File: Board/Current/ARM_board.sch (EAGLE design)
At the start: 177 parts, among them IC3 STM32F437VI, IC4 LM358DT, J1 USART/I2C, J10 ANALOG, J11 DGND, J12 DPWR, J13 DIGITAL, J14 SGND, J15 SPWR, J16 SERVO, J2 I2C2/USART3, J3 USART2, J5 SPI, J6 Bluesmirf, J7 SWD, J8 AGND, J9 APWR, Q1 STL4P2UH7, Q2 2STR1230, Q3 STL4P2UH7, SW1 SW, U1 LSM330, U10 BAV99, U11 BAV99, U12 USBLC6-2, U13 USBLC6-2, U14 STMPS2171MTR, U15 MC74HC164, U3 NC7SZU04, U4 L6206Q, U5 L6206Q, U6 SI7617, U7 SI7617, U8 SI7617, U9 SI7617, Y2 8MHz

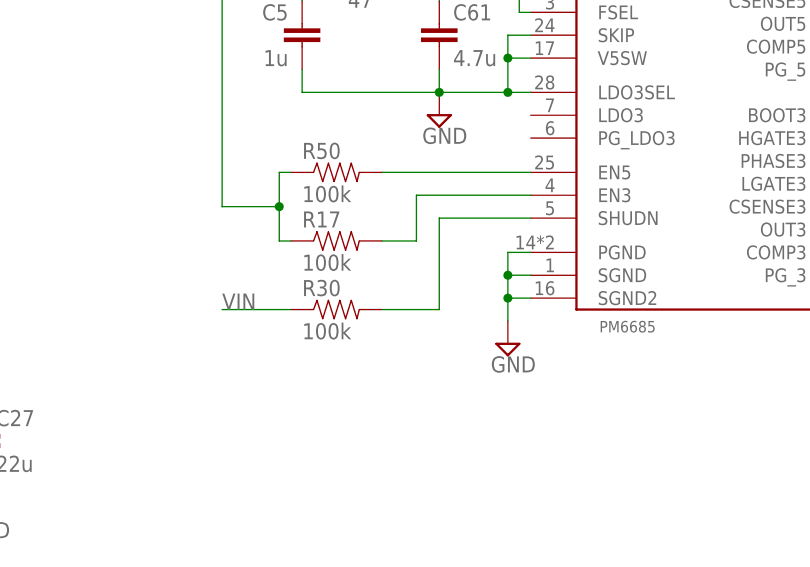
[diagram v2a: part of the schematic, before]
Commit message: Fixed the size of the 680uF capacitors. Added new voltage divider on SHDWN pin of switching controller.
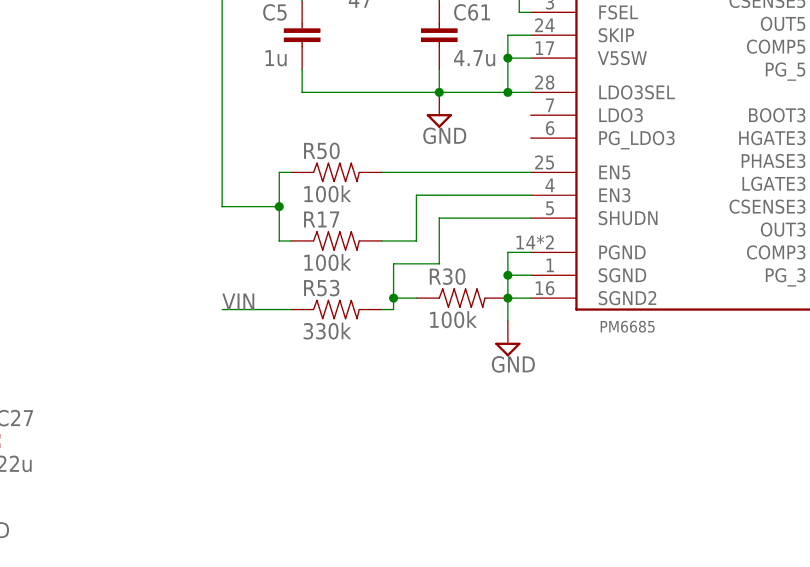
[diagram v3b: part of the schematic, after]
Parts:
- added R53: 330k, SparkFun:RESISTOR0402-RES
- C44, C52: device SparkFun:CAP_POLD -> SparkFun:CAP_POLE
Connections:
- net GND: now also R30.2
- net N$82: now also R30.1, R53.2; no longer R30.2
- net VIN: now also R53.1; no longer R30.1
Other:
- moved on the sheet: R30
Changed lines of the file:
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@@
 <grid distance="0.05" unitdist="inch" unit="inch" style="lines" multiple="1" display="no" altdistance="0.01" altunitdist="inch" altunit="inch"/>
 <layers>
-<layer number="1" name="Top" color="4" fill="1" visible="no" active="no"/>
-<layer number="16" name="Bottom" color="1" fill="1" visible="no" active="no"/>
-<layer number="17" name="Pads" color="2" fill="1" visible="no" active="no"/>
-<layer number="18" name="Vias" color="2" fill="1" visible="no" active="no"/>
-<layer number="19" name="Unrouted" color="6" fill="1" visible="no" active="no"/>
-<layer number="20" name="Dimension" color="15" fill="1" visible="no" active="no"/>
-<layer number="21" name="tPlace" color="15" fill="1" visible="no" active="no"/>
-<layer number="22" name="bPlace" color="7" fill="1" visible="no" active="no"/>
-<layer number="23" name="tOrigins" color="15" fill="1" visible="no" active="no"/>
-<layer number="24" name="bOrigins" color="15" fill="1" visible="no" active="no"/>
-<layer number="25" name="tNames" color="15" fill="1" visible="no" active="no"/>
-<layer number="26" name="bNames" color="7" fill="1" visible="no" active="no"/>
-<layer number="27" name="tValues" color="7" fill="1" visible="no" active="no"/>
-<layer number="28" name="bValues" color="7" fill="1" visible="no" active="no"/>
+<layer number="1" name="Top" color="4" fill="1" visible="yes" active="no"/>
+<layer number="16" name="Bottom" color="1" fill="1" visible="yes" active="no"/>
+<layer number="17" name="Pads" color="2" fill="1" visible="yes" active="no"/>
+<layer number="18" name="Vias" color="2" fill="1" visible="yes" active="no"/>
+<layer number="19" name="Unrouted" color="6" fill="1" visible="yes" active="no"/>
+<layer number="20" name="Dimension" color="15" fill="1" visible="yes" active="no"/>
+<layer number="21" name="tPlace" color="15" fill="1" visible="yes" active="no"/>
+<layer number="22" name="bPlace" color="7" fill="1" visible="yes" active="no"/>
+<layer number="23" name="tOrigins" color="15" fill="1" visible="yes" active="no"/>
+<layer number="24" name="bOrigins" color="15" fill="1" visible="yes" active="no"/>
+<layer number="25" name="tNames" color="15" fill="1" visible="yes" active="no"/>
+<layer number="26" name="bNames" color="7" fill="1" visible="yes" active="no"/>
+<layer number="27" name="tValues" color="7" fill="1" visible="yes" active="no"/>
+<layer number="28" name="bValues" color="7" fill="1" visible="yes" active="no"/>
 <layer number="29" name="tStop" color="7" fill="3" visible="no" active="no"/>
 <layer number="30" name="bStop" color="7" fill="6" visible="no" active="no"/>
@@
 <layer number="35" name="tGlue" color="7" fill="4" visible="no" active="no"/>
 <layer number="36" name="bGlue" color="7" fill="5" visible="no" active="no"/>
-<layer number="37" name="tTest" color="7" fill="1" visible="no" active="no"/>
-<layer number="38" name="bTest" color="7" fill="1" visible="no" active="no"/>
+<layer number="37" name="tTest" color="7" fill="1" visible="yes" active="no"/>
+<layer number="38" name="bTest" color="7" fill="1" visible="yes" active="no"/>
 <layer number="39" name="tKeepout" color="4" fill="11" visible="no" active="no"/>
 <layer number="40" name="bKeepout" color="1" fill="11" visible="no" active="no"/>
@@
 <layer number="44" name="Drills" color="7" fill="1" visible="no" active="no"/>
 <layer number="45" name="Holes" color="7" fill="1" visible="no" active="no"/>
-<layer number="46" name="Milling" color="3" fill="1" visible="no" active="no"/>
-<layer number="47" name="Measures" color="7" fill="1" visible="no" active="no"/>
-<layer number="48" name="Document" color="12" fill="1" visible="no" active="no"/>
-<layer number="49" name="Reference" color="7" fill="1" visible="no" active="no"/>
-<layer number="50" name="dxf" color="7" fill="1" visible="no" active="no"/>
-<layer number="51" name="tDocu" color="7" fill="1" visible="no" active="no"/>
-<layer number="52" name="bDocu" color="7" fill="1" visible="no" active="no"/>
-<layer number="53" name="tGND_GNDA" color="7" fill="9" visible="no" active="no"/>
-<layer number="54" name="bGND_GNDA" color="1" fill="9" visible="no" active="no"/>
-<layer number="56" name="wert" color="7" fill="1" visible="no" active="no"/>
+<layer number="46" name="Milling" color="3" fill="1" visible="yes" active="no"/>
+<layer number="47" name="Measures" color="7" fill="1" visible="yes" active="no"/>
+<layer number="48" name="Document" color="12" fill="1" visible="yes" active="no"/>
+<layer number="49" name="Reference" color="7" fill="1" visible="yes" active="no"/>
+<layer number="50" name="dxf" color="7" fill="1" visible="yes" active="no"/>
+<layer number="51" name="tDocu" color="7" fill="1" visible="yes" active="no"/>
+<layer number="52" name="bDocu" color="7" fill="1" visible="yes" active="no"/>
+<layer number="53" name="tGND_GNDA" color="7" fill="9" visible="yes" active="no"/>
+<layer number="54" name="bGND_GNDA" color="1" fill="9" visible="yes" active="no"/>
+<layer number="56" name="wert" color="7" fill="1" visible="yes" active="no"/>
 <layer number="91" name="Nets" color="2" fill="1" visible="yes" active="yes"/>
 <layer number="92" name="Busses" color="1" fill="1" visible="yes" active="yes"/>
@@
 <part name="C47" library="SparkFun" deviceset="CAP" device="0402-CAP" value="10n"/>
 <part name="C43" library="SparkFun" deviceset="CAP" device="0402-CAP" value="0.1u"/>
-<part name="C44" library="SparkFun" deviceset="CAP_POL" device="D" value="680uF"/>
+<part name="C44" library="SparkFun" deviceset="CAP_POL" device="E" value="680uF"/>
 <part name="U1" library="r_cubed" deviceset="LSM330" device=""/>
 <part name="SUPPLY36" library="supply2" deviceset="GND" device=""/>
@@
 <part name="SUPPLY58" library="supply2" deviceset="GND" device=""/>
 <part name="R8" library="SparkFun" deviceset="RESISTOR" device="0402-RES" value="510"/>
-<part name="C52" library="SparkFun" deviceset="CAP_POL" device="D" value="680uF"/>
+<part name="C52" library="SparkFun" deviceset="CAP_POL" device="E" value="680uF"/>
 <part name="U$3" library="SparkFun" deviceset="5V" device=""/>
 <part name="C53" library="SparkFun" deviceset="CAP" device="0402-CAP" value="47p"/>
@@
 <part name="R51" library="SparkFun" deviceset="RESISTOR" device="0402-RES" value="10"/>
 <part name="R52" library="SparkFun" deviceset="RESISTOR" device="0402-RES" value="10"/>
+<part name="R53" library="SparkFun" deviceset="RESISTOR" device="0402-RES" value="330k"/>
 </parts>
 <sheets>
@@
 <instance part="C61" gate="G$1" x="91.44" y="262.89"/>
 <instance part="R17" gate="G$1" x="80.01" y="241.3"/>
-<instance part="R30" gate="G$1" x="80.01" y="233.68"/>
+<instance part="R30" gate="G$1" x="93.98" y="234.95"/>
 <instance part="R50" gate="G$1" x="80.01" y="248.92"/>
 <instance part="SUPPLY69" gate="GND" x="91.44" y="255.27"/>
@@
 <instance part="R51" gate="G$1" x="144.78" y="290.83"/>
 <instance part="R52" gate="G$1" x="154.94" y="257.81"/>
+<instance part="R53" gate="G$1" x="80.01" y="233.68"/>
 </instances>
 <busses>
@@
 <junction x="99.06" y="237.49"/>
 <junction x="99.06" y="234.95"/>
+<pinref part="R30" gate="G$1" pin="2"/>
 </segment>
 <segment>
@@
 </segment>
 <segment>
-<pinref part="R30" gate="G$1" pin="1"/>
-<label x="67.31" y="233.68" size="1.778" layer="95"/>
-<wire x1="74.93" y1="233.68" x2="67.31" y2="233.68" width="0.1524" layer="91"/>
-</segment>
-<segment>
 <pinref part="R16" gate="G$1" pin="1"/>
 <wire x1="85.09" y1="302.26" x2="78.74" y2="302.26" width="0.1524" layer="91"/>
@@
 <junction x="78.74" y="302.26"/>
 </segment>
+<segment>
+<pinref part="R53" gate="G$1" pin="1"/>
+<wire x1="74.93" y1="233.68" x2="67.31" y2="233.68" width="0.1524" layer="91"/>
+<label x="67.31" y="233.68" size="1.778" layer="95"/>
+</segment>
 </net>
 <net name="N$29" class="0">
@@
 <net name="N$82" class="0">
 <segment>
-<pinref part="R30" gate="G$1" pin="2"/>
-<wire x1="91.44" y1="233.68" x2="85.09" y2="233.68" width="0.1524" layer="91"/>
 <pinref part="U$1" gate="G$1" pin="SHUDN"/>
 <wire x1="101.6" y1="243.84" x2="91.44" y2="243.84" width="0.1524" layer="91"/>
-<wire x1="91.44" y1="243.84" x2="91.44" y2="233.68" width="0.1524" layer="91"/>
+<wire x1="91.44" y1="243.84" x2="91.44" y2="238.76" width="0.1524" layer="91"/>
+<wire x1="91.44" y1="238.76" x2="86.36" y2="238.76" width="0.1524" layer="91"/>
+<wire x1="86.36" y1="238.76" x2="86.36" y2="234.95" width="0.1524" layer="91"/>
+<pinref part="R30" gate="G$1" pin="1"/>
+<wire x1="88.9" y1="234.95" x2="86.36" y2="234.95" width="0.1524" layer="91"/>
+<pinref part="R53" gate="G$1" pin="2"/>
+<wire x1="85.09" y1="233.68" x2="86.36" y2="233.68" width="0.1524" layer="91"/>
+<wire x1="86.36" y1="233.68" x2="86.36" y2="234.95" width="0.1524" layer="91"/>
+<junction x="86.36" y="234.95"/>
 </segment>
 </net>

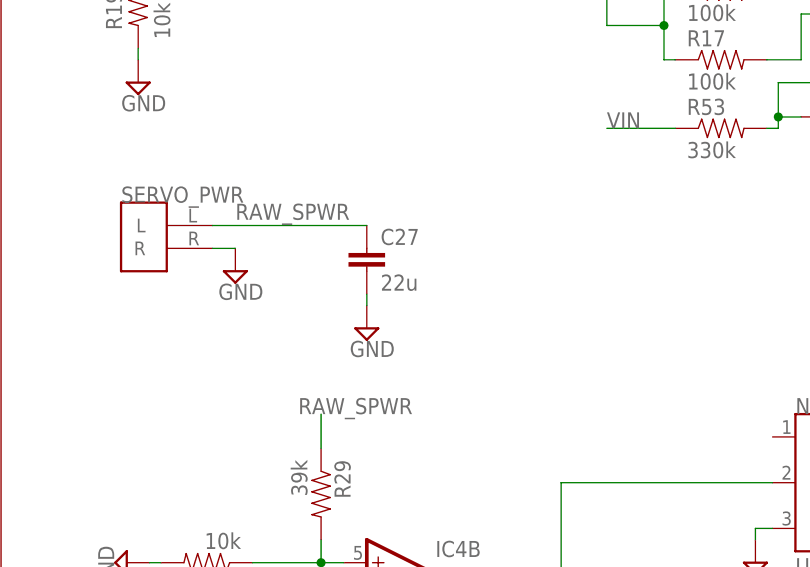
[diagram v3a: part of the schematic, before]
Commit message: Went through the size of all the passives.
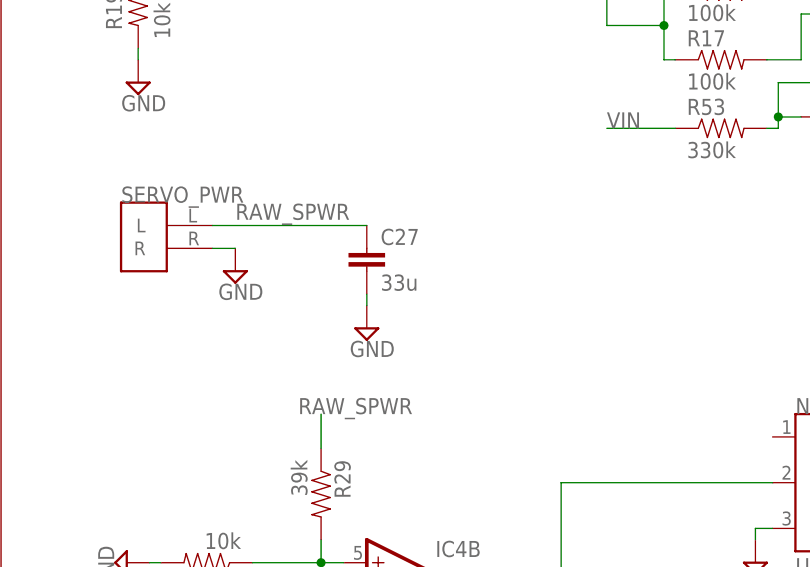
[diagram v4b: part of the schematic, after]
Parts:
- C27: value 22u -> 33u; device SparkFun:CAP1206 -> SparkFun:CAP0805
- C28, C6: device SparkFun:CAP0603-CAP -> SparkFun:CAP0805
- C39: device SparkFun:CAP0603-CAP -> SparkFun:CAP0402-CAP
- C44, C52: device SparkFun:CAP_POLE -> SparkFun:CAP_POLD
- C59: device SparkFun:CAP0402-CAP -> SparkFun:CAP0603-CAP
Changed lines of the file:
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@@
 <setting verticaltext="up"/>
 </settings>
-<grid distance="0.05" unitdist="inch" unit="inch" style="lines" multiple="1" display="no" altdistance="0.01" altunitdist="inch" altunit="inch"/>
+<grid distance="0.1" unitdist="inch" unit="inch" style="lines" multiple="1" display="no" altdistance="0.01" altunitdist="inch" altunit="inch"/>
 <layers>
 <layer number="1" name="Top" color="4" fill="1" visible="yes" active="no"/>
@@
 <part name="SUPPLY39" library="supply2" deviceset="GND" device=""/>
 <part name="+3V5" library="supply1" deviceset="+3V3" device=""/>
-<part name="C27" library="SparkFun" deviceset="CAP" device="1206" value="22u"/>
+<part name="C27" library="SparkFun" deviceset="CAP" device="0805" value="33u"/>
 <part name="U3" library="SparkFun" deviceset="INVERTER" device="&quot;&quot;" value="NC7SZU04"/>
 <part name="SUPPLY40" library="supply2" deviceset="GND" device=""/>
@@
 <part name="SUPPLY42" library="supply2" deviceset="GND" device=""/>
 <part name="J5" library="SparkFun" deviceset="M06" device="SIP" value="SPI"/>
-<part name="C6" library="SparkFun" deviceset="CAP" device="0603-CAP" value="33u"/>
+<part name="C6" library="SparkFun" deviceset="CAP" device="0805" value="33u"/>
 <part name="C30" library="SparkFun" deviceset="CAP" device="0402-CAP" value="10n"/>
 <part name="R36" library="SparkFun" deviceset="RESISTOR" device="0402-RES" value="100k"/>
@@
 <part name="SD" library="SparkFun" deviceset="USD-SOCKET" device="NEW"/>
 <part name="+3V10" library="supply1" deviceset="+3V3" device=""/>
-<part name="C39" library="SparkFun" deviceset="CAP" device="0603-CAP" value="4.7u"/>
+<part name="C39" library="SparkFun" deviceset="CAP" device="0402-CAP" value="4.7u"/>
 <part name="C40" library="SparkFun" deviceset="CAP" device="0402-CAP" value="0.1u"/>
 <part name="C41" library="SparkFun" deviceset="CAP" device="0402-CAP" value="0.1u"/>
@@
 <part name="C47" library="SparkFun" deviceset="CAP" device="0402-CAP" value="10n"/>
 <part name="C43" library="SparkFun" deviceset="CAP" device="0402-CAP" value="0.1u"/>
-<part name="C44" library="SparkFun" deviceset="CAP_POL" device="E" value="680uF"/>
+<part name="C44" library="SparkFun" deviceset="CAP_POL" device="D" value="680uF"/>
 <part name="U1" library="r_cubed" deviceset="LSM330" device=""/>
 <part name="SUPPLY36" library="supply2" deviceset="GND" device=""/>
@@
 <part name="SUPPLY58" library="supply2" deviceset="GND" device=""/>
 <part name="R8" library="SparkFun" deviceset="RESISTOR" device="0402-RES" value="510"/>
-<part name="C52" library="SparkFun" deviceset="CAP_POL" device="E" value="680uF"/>
+<part name="C52" library="SparkFun" deviceset="CAP_POL" device="D" value="680uF"/>
 <part name="U$3" library="SparkFun" deviceset="5V" device=""/>
 <part name="C53" library="SparkFun" deviceset="CAP" device="0402-CAP" value="47p"/>
@@
 <part name="D2" library="SparkFun" deviceset="DIODE-SCHOTTKY" device="A" value="STPS1L30M"/>
 <part name="R16" library="SparkFun" deviceset="RESISTOR" device="0402-RES" value="3.9"/>
-<part name="C59" library="SparkFun" deviceset="CAP" device="0402-CAP" value="4.7u"/>
+<part name="C59" library="SparkFun" deviceset="CAP" device="0603-CAP" value="4.7u"/>
 <part name="C60" library="SparkFun" deviceset="CAP" device="0402-CAP" value="0.1u"/>
 <part name="C61" library="SparkFun" deviceset="CAP" device="0402-CAP" value="4.7u"/>
@@
 <part name="D3" library="r_cubed" deviceset="SOD-23" device=""/>
 <part name="C26" library="SparkFun" deviceset="CAP" device="1206" value="33u"/>
-<part name="C28" library="SparkFun" deviceset="CAP" device="0603-CAP" value="33u"/>
+<part name="C28" library="SparkFun" deviceset="CAP" device="0805" value="33u"/>
 <part name="C32" library="SparkFun" deviceset="CAP" device="0402-CAP" value="0.1u"/>
 <part name="R33" library="SparkFun" deviceset="RESISTOR" device="0402-RES" value="1k"/>

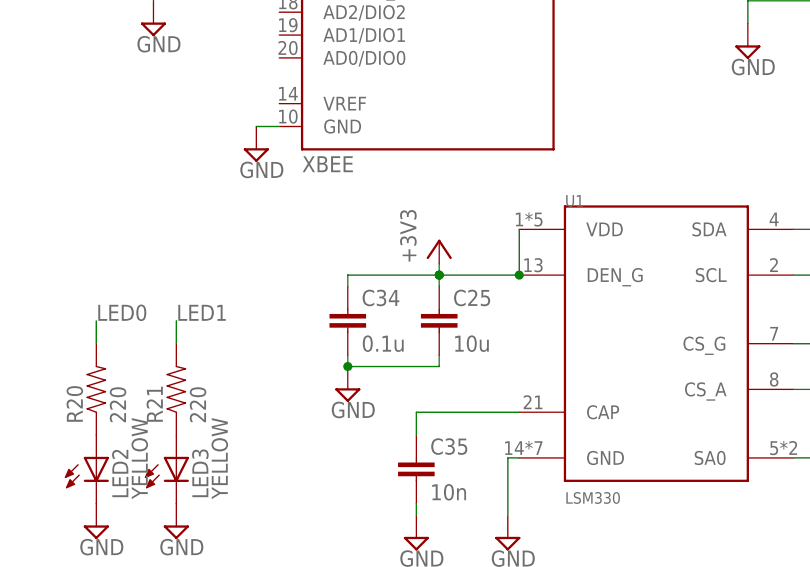
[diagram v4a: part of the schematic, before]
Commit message: Added more capacitors to the gyro.
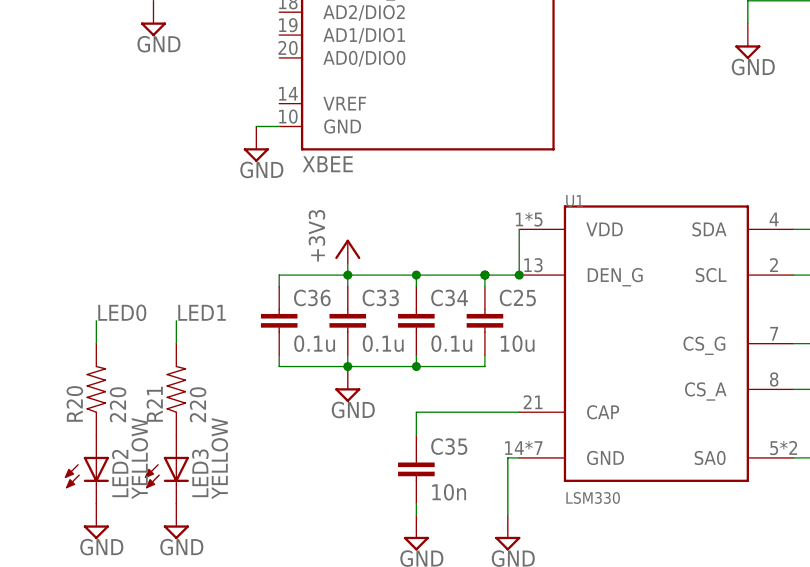
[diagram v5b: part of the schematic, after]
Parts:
- added C33, C36: 0.1u, SparkFun:CAP0402-CAP
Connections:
- net +3V3: now also C33.1, C36.1
- net GND: now also C33.2, C36.2
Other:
- moved on the sheet: C25, C34
